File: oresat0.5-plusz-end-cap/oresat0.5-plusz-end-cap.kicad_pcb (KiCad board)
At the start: 2 copper layers, 105.6 x 105.6 mm, 41 parts

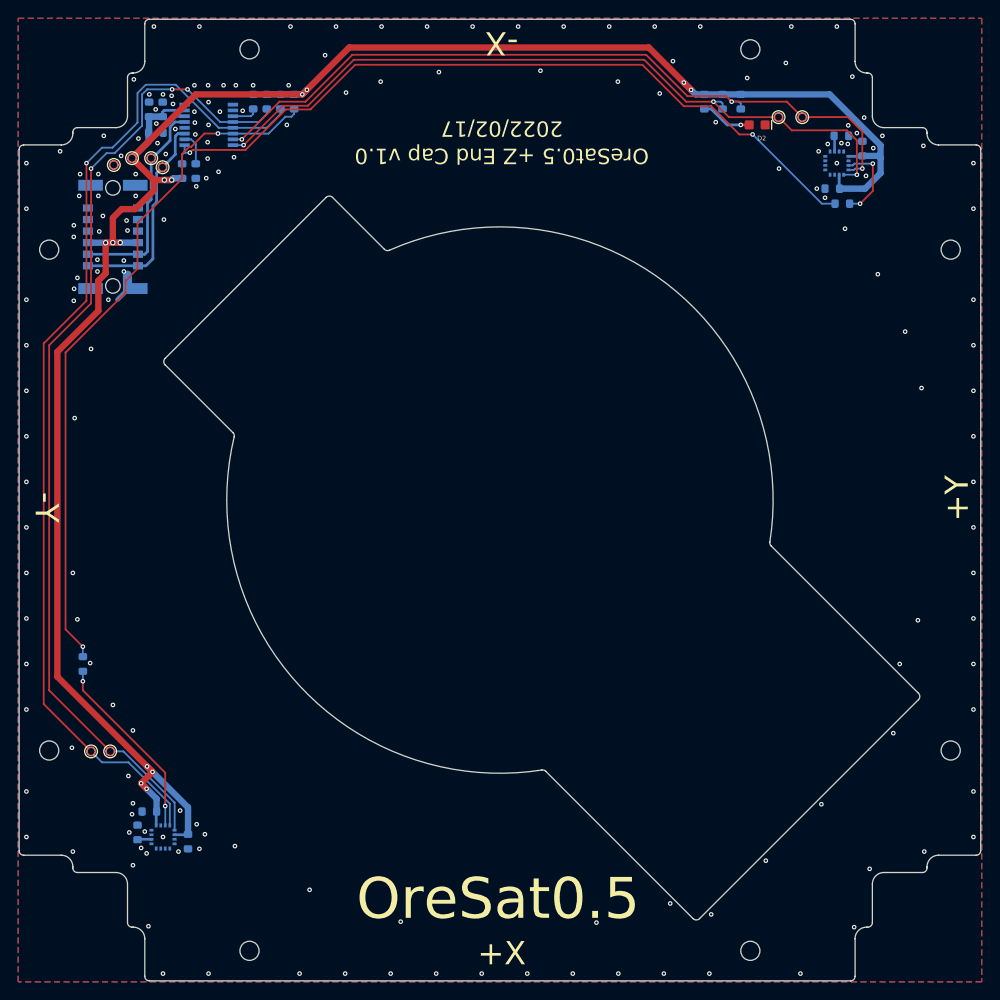
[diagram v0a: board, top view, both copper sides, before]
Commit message: Updated both oresat0.5 end caps. Fixed layout, and added patch antennas
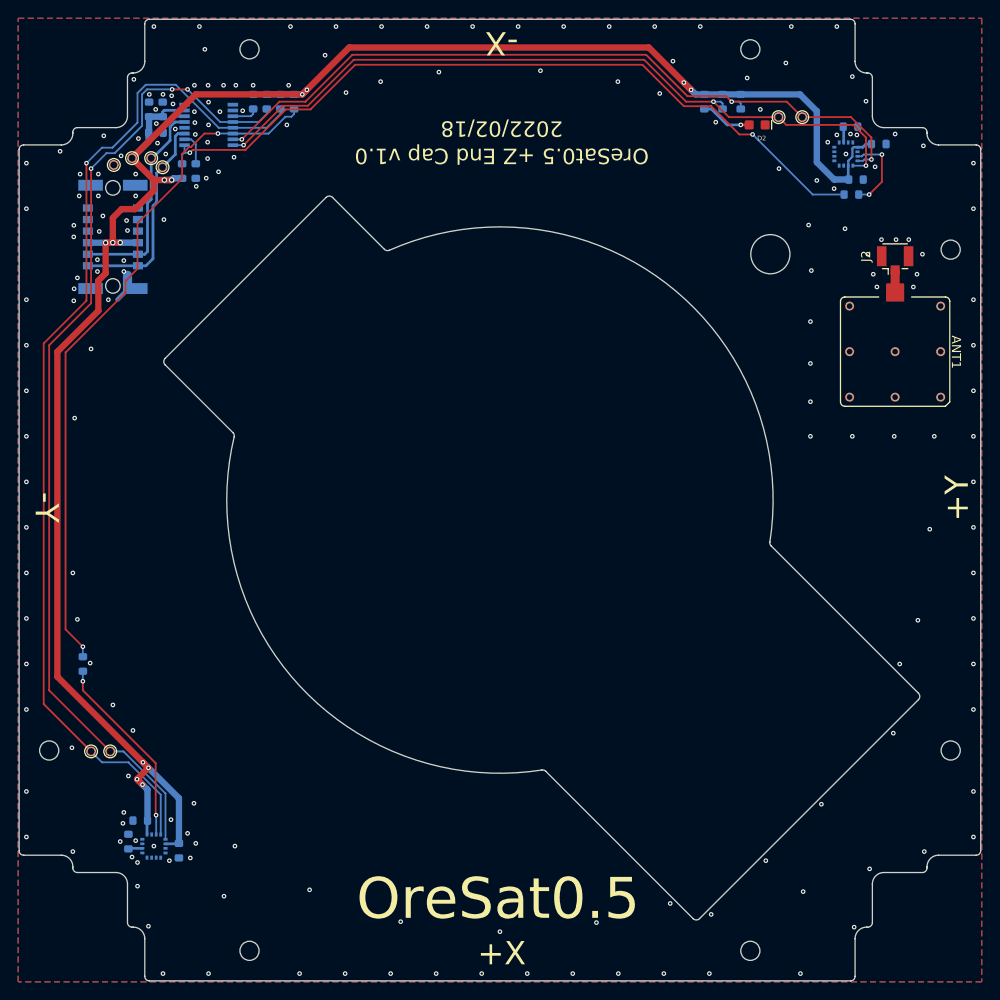
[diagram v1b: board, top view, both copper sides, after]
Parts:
- removed @HOLE5: , 
- added ANT1: ANT1008, oresat-misc:RFMi-ANT1008-S-Band-Patch, F.Cu at (191.9, 88.7)
- added J2: U.FL-R-SMA, Connector_Coaxial:U.FL_Hirose_U.FL-R-SMT-1_Vertical, F.Cu at (191.9, 78.7)
- added REF**: MountingHole_4.3mm_M4, MountingHole:MountingHole_4.3mm_M4, F.Cu at (178.2, 78.0)
- moved C1 2.79 mm to (187.6, 69.8), turned to 0 degrees
- moved C10 1.87 mm to (190.1, 65.9), turned to 0 degrees
- moved C12 1.41 mm to (107.7, 142.5)
- moved C13 1.41 mm to (187.0, 64.0)
- moved C2 1.41 mm to (113.2, 143.5)
- moved C7 1.41 mm to (109.0, 140.2)
- moved R12 1.41 mm to (187.1, 71.5)
- moved U2 1.41 mm to (186.5, 67.0)
- moved U3 1.41 mm to (110.5, 143.0)
- renumbered CF2 to J1
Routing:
- net 3.3V: track 228.2 -> 223.8 mm
- net Net-(ANT1-Pad1): track 0.00 -> 2.45 mm
- net Net-(R11-Pad1): track 20.7 -> 21.3 mm
- net Net-(R12-Pad2): track 83.9 -> 84.5 mm
- net /SDA1: track 112.0 -> 112.6 mm
- net /SCL1: track 108.4 -> 109.0 mm
- net GND: vias 179 -> 198
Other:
- board text added: "2022/02/18"
- board text removed: "2022/02/17"

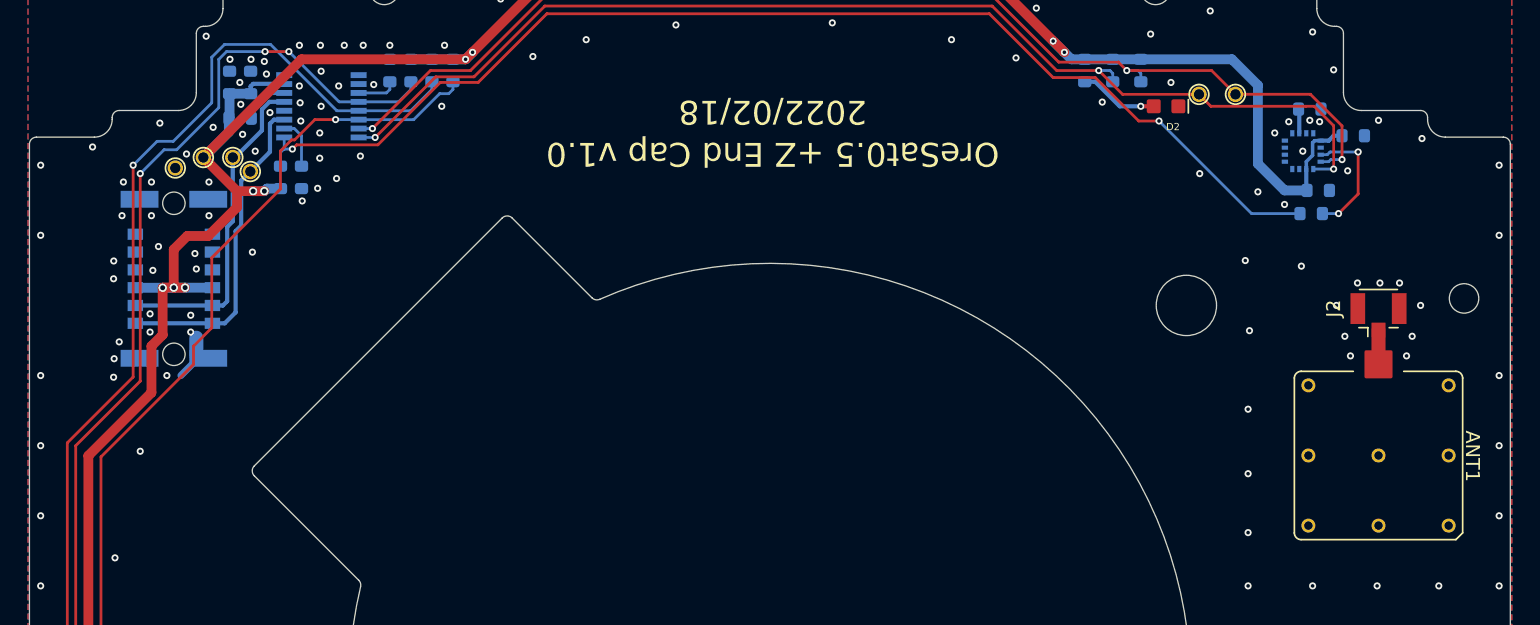
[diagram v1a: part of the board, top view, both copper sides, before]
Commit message: Updated both OreSat0.5 end caps and cleaned up errors
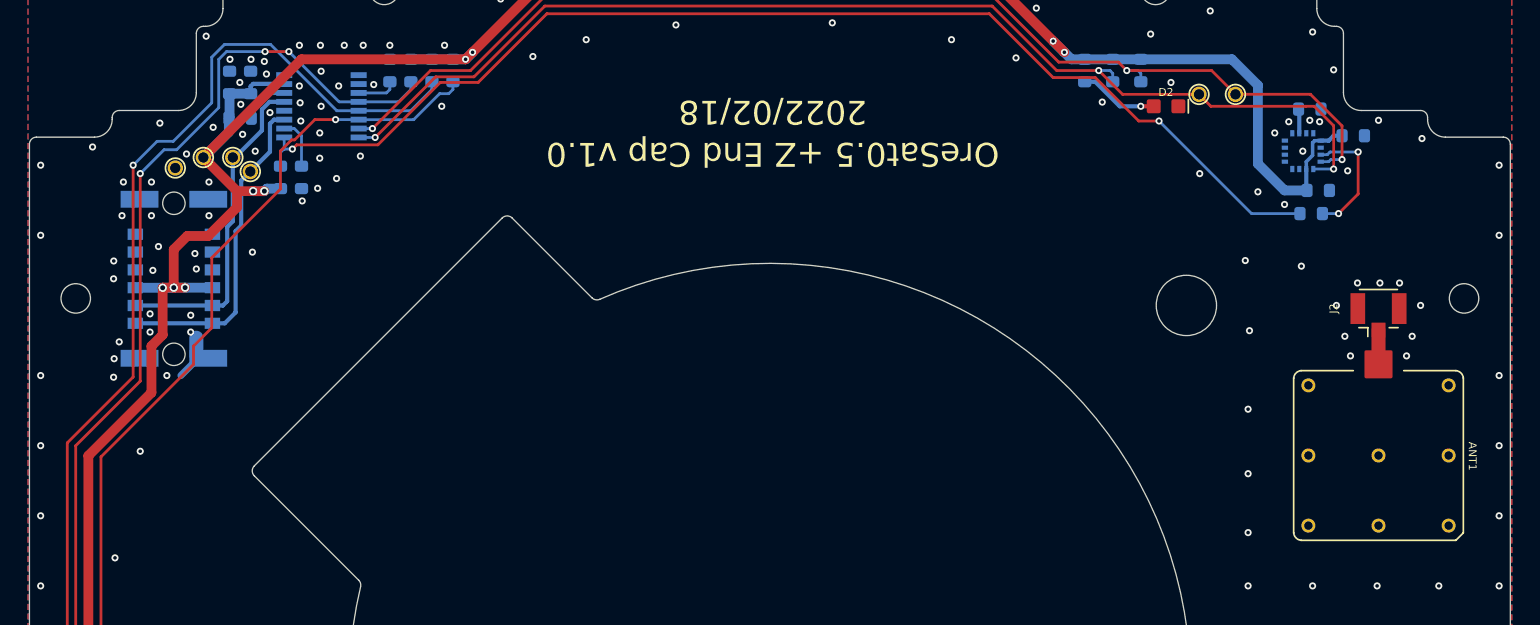
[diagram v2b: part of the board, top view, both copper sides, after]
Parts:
- added @HOLE4: MountingHole_2.1mm, MountingHole:MountingHole_2.1mm, F.Cu at (99.0, 77.5)
- @HOLE0, @HOLE1, @HOLE2, @HOLE3, @HOLE4, @HOLE6, @HOLE7: value (none) -> MountingHole_2.1mm; footprint (none) -> MountingHole:MountingHole_2.1mm
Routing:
- net GND: track 5.54 -> 3.42 mm

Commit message: OreSat0.5 end caps design review fixes
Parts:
- U1: value (none) -> LTC4305
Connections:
- net /I2C-SCL renamed /MAG-SCL
- net /I2C-SDA renamed /MAG-SDA
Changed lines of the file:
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@@
   (net 3 "Net-(C12-Pad1)")
   (net 4 "Net-(C13-Pad1)")
-  (net 5 "/I2C-SDA")
-  (net 6 "/I2C-SCL")
+  (net 5 "/MAG-SCL")
+  (net 6 "/MAG-SDA")
   (net 7 "unconnected-(J1-Pad9)")
   (net 8 "unconnected-(J1-Pad10)")
@@
       ) (layer "F.Fab") (width 0) (fill solid))
     (pad "1" thru_hole circle (at 0 0 270) (size 1.1 1.1) (drill 0.7366) (layers *.Cu *.Mask)
-      (net 6 "/I2C-SCL") (pinfunction "1") (pintype "passive") (solder_mask_margin 0.0635))
+      (net 5 "/MAG-SCL") (pinfunction "1") (pintype "passive") (solder_mask_margin 0.0635))
   )
   (footprint "oresat0-plusz-end-cap:1X01" (layer "F.Cu")
@@
       ) (layer "F.Fab") (width 0) (fill solid))
     (pad "1" thru_hole circle (at 0 0 270) (size 1.1 1.1) (drill 0.7366) (layers *.Cu *.Mask)
-      (net 5 "/I2C-SDA") (pinfunction "1") (pintype "passive") (solder_mask_margin 0.0635))
+      (net 6 "/MAG-SDA") (pinfunction "1") (pintype "passive") (solder_mask_margin 0.0635))
   )
   (footprint "MountingHole:MountingHole_4.3mm_M4" (layer "F.Cu")
@@
     (pad "" np_thru_hole circle locked (at 5.385 0 270) (size 1.6 1.6) (drill 1.6) (layers *.Cu *.Mask))
     (pad "1" smd rect locked (at 3.175 -2.75 90) (size 0.8 1.1) (layers "B.Cu" "B.Paste" "B.Mask")
-      (net 5 "/I2C-SDA") (pinfunction "1") (pintype "passive") (solder_mask_margin 0.0635))
+      (net 6 "/MAG-SDA") (pinfunction "1") (pintype "passive") (solder_mask_margin 0.0635))
     (pad "2" smd rect locked (at 3.175 2.75 90) (size 0.8 1.1) (layers "B.Cu" "B.Paste" "B.Mask")
-      (net 5 "/I2C-SDA") (pinfunction "2") (pintype "passive") (solder_mask_margin 0.0635))
+      (net 6 "/MAG-SDA") (pinfunction "2") (pintype "passive") (solder_mask_margin 0.0635))
     (pad "3" smd rect locked (at 1.905 -2.75 90) (size 0.8 1.1) (layers "B.Cu" "B.Paste" "B.Mask")
-      (net 6 "/I2C-SCL") (pinfunction "3") (pintype "passive") (solder_mask_margin 0.0635))
+      (net 5 "/MAG-SCL") (pinfunction "3") (pintype "passive") (solder_mask_margin 0.0635))
     (pad "4" smd rect locked (at 1.905 2.75 90) (size 0.8 1.1) (layers "B.Cu" "B.Paste" "B.Mask")
-      (net 6 "/I2C-SCL") (pinfunction "4") (pintype "passive") (solder_mask_margin 0.0635))
+      (net 5 "/MAG-SCL") (pinfunction "4") (pintype "passive") (solder_mask_margin 0.0635))
     (pad "5" smd rect locked (at 0.635 -2.75 90) (size 0.8 1.1) (layers "B.Cu" "B.Paste" "B.Mask")
       (net 1 "3.3V") (pinfunction "5") (pintype "passive") (solder_mask_margin 0.0635))
@@
       (net 2 "GND") (pinfunction "8") (pintype "passive") (solder_mask_margin 0.0635))
     (pad "9" smd rect locked (at -1.905 -2.75 90) (size 0.8 1.1) (layers "B.Cu" "B.Paste" "B.Mask")
-      (net 7 "unconnected-(J1-Pad9)") (pinfunction "9") (pintype "passive") (solder_mask_margin 0.0635))
+      (net 7 "unconnected-(J1-Pad9)") (pinfunction "9") (pintype "passive+no_connect") (solder_mask_margin 0.0635))
     (pad "10" smd rect locked (at -1.905 2.75 90) (size 0.8 1.1) (layers "B.Cu" "B.Paste" "B.Mask")
-      (net 8 "unconnected-(J1-Pad10)") (pinfunction "10") (pintype "passive") (solder_mask_margin 0.0635))
+      (net 8 "unconnected-(J1-Pad10)") (pinfunction "10") (pintype "passive+no_connect") (solder_mask_margin 0.0635))
     (pad "11" smd rect locked (at -3.175 -2.75 90) (size 0.8 1.1) (layers "B.Cu" "B.Paste" "B.Mask")
-      (net 9 "unconnected-(J1-Pad11)") (pinfunction "11") (pintype "passive") (solder_mask_margin 0.0635))
+      (net 9 "unconnected-(J1-Pad11)") (pinfunction "11") (pintype "passive+no_connect") (solder_mask_margin 0.0635))
     (pad "12" smd rect locked (at -3.175 2.75 90) (size 0.8 1.1) (layers "B.Cu" "B.Paste" "B.Mask")
-      (net 22 "unconnected-(J1-Pad12)") (pinfunction "12") (pintype "passive") (solder_mask_margin 0.0635))
+      (net 22 "unconnected-(J1-Pad12)") (pinfunction "12") (pintype "passive+no_connect") (solder_mask_margin 0.0635))
     (pad "P$1" smd rect locked (at -5.67 -2.45 180) (size 2.7 1.2) (layers "B.Cu" "B.Paste" "B.Mask")
       (net 2 "GND") (pinfunction "SHIELDS") (pintype "passive") (solder_mask_margin 0.0635))
@@
     (property "Sheetfile" "File: oresat0.5-plusz-end-cap.kicad_sch")
     (property "Sheetname" "")
-    (property "Value" "")
+    (property "Value" "LTC4305")
     (fp_text reference "U1" (at 3 0.88) (layer "B.SilkS")
       (effects (font (size 0.56 0.56) (thickness 0.12)) (justify right mirror))
     )
-    (fp_text value "LTC4305IGN" (at -2.286 -4.318 90) (layer "B.Fab")
+    (fp_text value "LTC4305" (at -2.286 -4.318 90) (layer "B.Fab")
       (effects (font (size 0.726968 0.726968) (thickness 0.085832)) (justify left mirror))
     )
@@
       (net 11 "Net-(R1-Pad2)") (pinfunction "~{ALERT}") (pintype "output") (solder_mask_margin 0.0635))
     (pad "3" smd rect (at -0.9525 -2.6543) (size 1.143 0.4191) (layers "B.Cu" "B.Paste" "B.Mask")
-      (net 5 "/I2C-SDA") (pinfunction "SDAIN") (pintype "bidirectional") (solder_mask_margin 0.0635))
+      (net 6 "/MAG-SDA") (pinfunction "SDAIN") (pintype "bidirectional") (solder_mask_margin 0.0635))
     (pad "4" smd rect (at -0.3175 -2.6543) (size 1.143 0.4191) (layers "B.Cu" "B.Paste" "B.Mask")
       (net 2 "GND") (pinfunction "GND") (pintype "power_in") (solder_mask_margin 0.0635))
     (pad "5" smd rect (at 0.3175 -2.6543) (size 1.143 0.4191) (layers "B.Cu" "B.Paste" "B.Mask")
-      (net 6 "/I2C-SCL") (pinfunction "SCLIN") (pintype "bidirectional") (solder_mask_margin 0.0635))
+      (net 5 "/MAG-SCL") (pinfunction "SCLIN") (pintype "bidirectional") (solder_mask_margin 0.0635))
     (pad "6" smd rect (at 0.9525 -2.6543) (size 1.143 0.4191) (layers "B.Cu" "B.Paste" "B.Mask")
       (net 19 "Net-(R10-Pad1)") (pinfunction "ENABLE") (pintype "input") (solder_mask_margin 0.0635))
@@
   (segment (start 186.25 65.725) (end 186.25 64.05) (width 0.3) (layer "B.Cu") (net 4))
   (segment (start 186.25 64.05) (end 186.2 64) (width 0.3) (layer "B.Cu") (net 4))
-  (segment (start 112.85 67.05) (end 112.85 65.044494) (width 0.3) (layer "B.Cu") (net 5))
-  (segment (start 110.8 72.3) (end 110.8 69.1) (width 0.3) (layer "B.Cu") (net 5))
-  (segment (start 110.8 69.1) (end 111.45 68.45) (width 0.3) (layer "B.Cu") (net 5))
-  (segment (start 109.625 79.275) (end 110.4 78.5) (width 0.3) (layer "B.Cu") (net 5))
-  (segment (start 110.4 72.7) (end 110.8 72.3) (width 0.3) (layer "B.Cu") (net 5))
-  (segment (start 113.141993 64.7525) (end 113.8657 64.7525) (width 0.3) (layer "B.Cu") (net 5))
-  (segment (start 112.85 65.044494) (end 113.141993 64.7525) (width 0.3) (layer "B.Cu") (net 5))
-  (segment (start 108.75 79.275) (end 103.25 79.275) (width 0.3) (layer "B.Cu") (net 5))
-  (segment (start 108.75 79.275) (end 109.625 79.275) (width 0.3) (layer "B.Cu") (net 5))
-  (segment (start 111.45 68.45) (end 112.85 67.05) (width 0.3) (layer "B.Cu") (net 5))
-  (segment (start 110.4 78.5) (end 110.4 72.7) (width 0.3) (layer "B.Cu") (net 5))
-  (segment (start 108.75 78.005) (end 103.25 78.005) (width 0.3) (layer "B.Cu") (net 6))
-  (segment (start 109.497668 78.005) (end 109.8 77.702669) (width 0.3) (layer "B.Cu") (net 6))
-  (segment (start 109.8 77.702669) (end 109.8 72.4) (width 0.3) (layer "B.Cu") (net 6))
-  (segment (start 110.2 72) (end 110.2 67.45) (width 0.3) (layer "B.Cu") (net 6))
-  (segment (start 109.8 72.4) (end 110.2 72) (width 0.3) (layer "B.Cu") (net 6))
-  (segment (start 112.8175 63.4825) (end 113.8657 63.4825) (width 0.3) (layer "B.Cu") (net 6))
-  (segment (start 110.2 67.45) (end 110.35 67.45) (width 0.3) (layer "B.Cu") (net 6))
-  (segment (start 108.75 78.005) (end 109.497668 78.005) (width 0.3) (layer "B.Cu") (net 6))
-  (segment (start 112.28 64.02) (end 112.8175 63.4825) (width 0.3) (layer "B.Cu") (net 6))
-  (segment (start 112.28 65.52) (end 112.28 64.02) (width 0.3) (layer "B.Cu") (net 6))
-  (segment (start 112.28 65.52) (end 110.35 67.45) (width 0.3) (layer "B.Cu") (net 6))
+  (segment (start 108.75 78.005) (end 103.25 78.005) (width 0.3) (layer "B.Cu") (net 5))
+  (segment (start 109.497668 78.005) (end 109.8 77.702669) (width 0.3) (layer "B.Cu") (net 5))
+  (segment (start 109.8 77.702669) (end 109.8 72.4) (width 0.3) (layer "B.Cu") (net 5))
+  (segment (start 110.2 72) (end 110.2 67.45) (width 0.3) (layer "B.Cu") (net 5))
+  (segment (start 109.8 72.4) (end 110.2 72) (width 0.3) (layer "B.Cu") (net 5))
+  (segment (start 112.8175 63.4825) (end 113.8657 63.4825) (width 0.3) (layer "B.Cu") (net 5))
+  (segment (start 110.2 67.45) (end 110.35 67.45) (width 0.3) (layer "B.Cu") (net 5))
+  (segment (start 108.75 78.005) (end 109.497668 78.005) (width 0.3) (layer "B.Cu") (net 5))
+  (segment (start 112.28 64.02) (end 112.8175 63.4825) (width 0.3) (layer "B.Cu") (net 5))
+  (segment (start 112.28 65.52) (end 112.28 64.02) (width 0.3) (layer "B.Cu") (net 5))
+  (segment (start 112.28 65.52) (end 110.35 67.45) (width 0.3) (layer "B.Cu") (net 5))
+  (segment (start 112.85 67.05) (end 112.85 65.044494) (width 0.3) (layer "B.Cu") (net 6))
+  (segment (start 110.8 72.3) (end 110.8 69.1) (width 0.3) (layer "B.Cu") (net 6))
+  (segment (start 110.8 69.1) (end 111.45 68.45) (width 0.3) (layer "B.Cu") (net 6))
+  (segment (start 109.625 79.275) (end 110.4 78.5) (width 0.3) (layer "B.Cu") (net 6))
+  (segment (start 110.4 72.7) (end 110.8 72.3) (width 0.3) (layer "B.Cu") (net 6))
+  (segment (start 113.141993 64.7525) (end 113.8657 64.7525) (width 0.3) (layer "B.Cu") (net 6))
+  (segment (start 112.85 65.044494) (end 113.141993 64.7525) (width 0.3) (layer "B.Cu") (net 6))
+  (segment (start 108.75 79.275) (end 103.25 79.275) (width 0.3) (layer "B.Cu") (net 6))
+  (segment (start 108.75 79.275) (end 109.625 79.275) (width 0.3) (layer "B.Cu") (net 6))
+  (segment (start 111.45 68.45) (end 112.85 67.05) (width 0.3) (layer "B.Cu") (net 6))
+  (segment (start 110.4 78.5) (end 110.4 72.7) (width 0.3) (layer "B.Cu") (net 6))
   (segment (start 174.95 63.8) (end 175.873 63.8) (width 0.3) (layer "F.Cu") (net 10))
   (via (at 174.95 63.8) (size 0.508) (drill 0.254) (layers "F.Cu" "B.Cu") (net 10))
